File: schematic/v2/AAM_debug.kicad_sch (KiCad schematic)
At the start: 16 parts, among them J16 AAM_DBG, J20 USB_A, U33 CH340G, Y2 Crystal

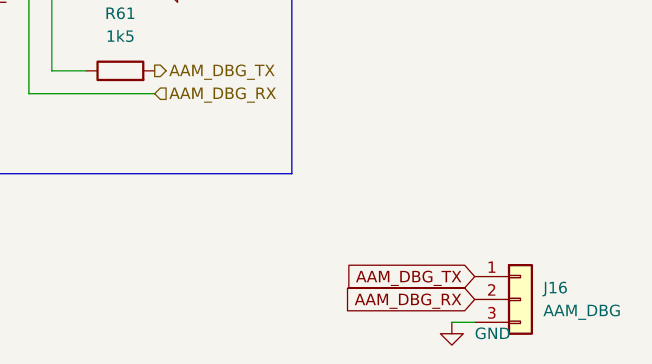
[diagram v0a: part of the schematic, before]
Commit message: progress on putting things in different sheets
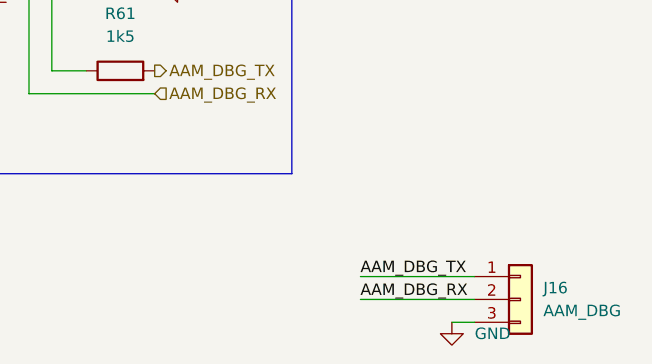
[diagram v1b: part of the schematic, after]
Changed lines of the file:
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@@
+	(wire
+		(pts
+			(xy 179.07 113.03) (xy 191.77 113.03)
+		)
+		(stroke
+			(width 0)
+			(type default)
+		)
+	)
 	(wire
 		(pts
@@
 	(wire
 		(pts
+			(xy 179.07 110.49) (xy 191.77 110.49)
+		)
+		(stroke
+			(width 0)
+			(type default)
+		)
+	)
+	(wire
+		(pts
 			(xy 127 48.26) (xy 127 52.07)
 		)
@@
 		)
 	)
-	(global_label "AAM_DBG_RX"
-		(shape input)
-		(at 191.77 113.03 180)
-		(fields_autoplaced yes)
+	(label "AAM_DBG_RX"
+		(at 179.07 113.03 0)
 		(effects
 			(font
 				(size 1.27 1.27)
 			)
-			(justify right)
-		)
-		(property "Intersheetrefs" "${INTERSHEET_REFS}"
-			(at 176.6292 113.03 0)
-			(effects
-				(font
-					(size 1.27 1.27)
-				)
-				(justify right)
-				(hide yes)
+			(justify left bottom)
+		)
+	)
+	(label "AAM_DBG_TX"
+		(at 179.07 110.49 0)
+		(effects
+			(font
+				(size 1.27 1.27)
 			)
+			(justify left bottom)
 		)
 	)
@@
 				(hide yes)
 			)
-		)
-	)
-	(global_label "AAM_DBG_TX"
-		(shape input)
-		(at 191.77 110.49 180)
-		(fields_autoplaced yes)
-		(effects
-			(font
-				(size 1.27 1.27)
-			)
-			(justify right)
-		)
-		(property "Intersheetrefs" "${INTERSHEET_REFS}"
-			(at 176.9316 110.49 0)
-			(effects
-				(font
-					(size 1.27 1.27)
-				)
-				(justify right)
-				(hide yes)
-			)

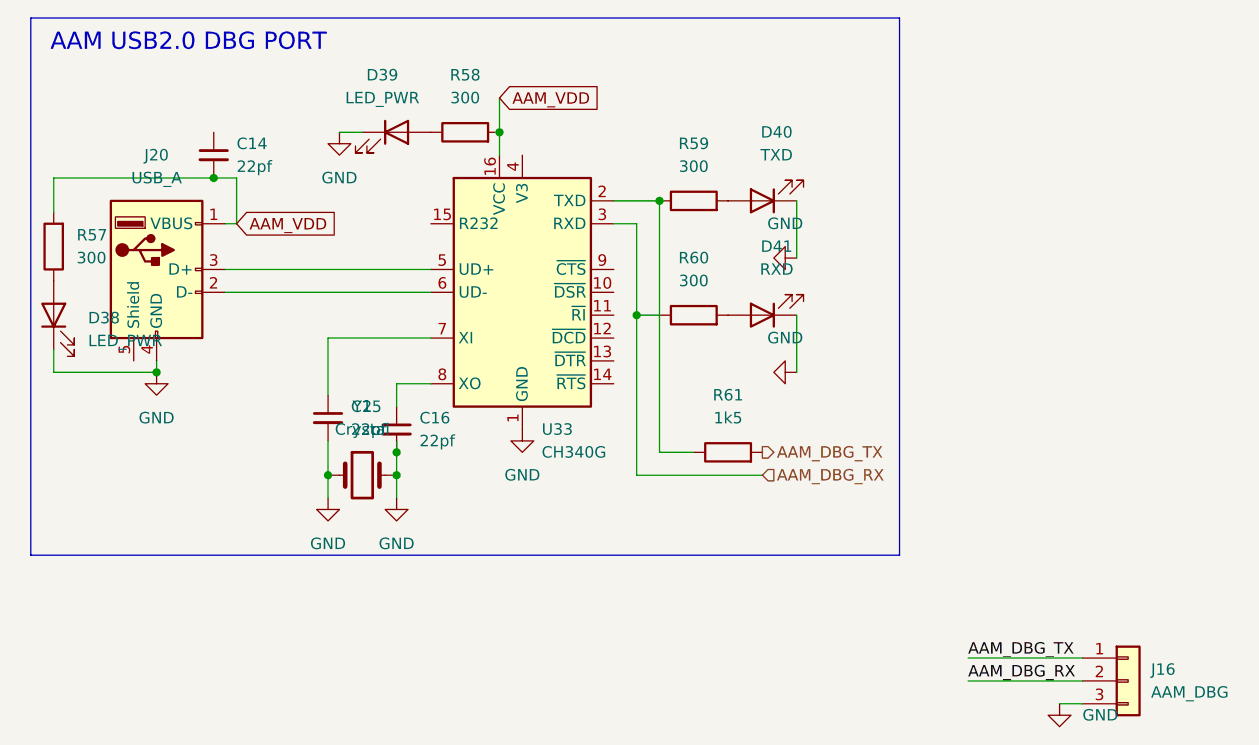
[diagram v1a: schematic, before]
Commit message: v2 updates. remove sniffer
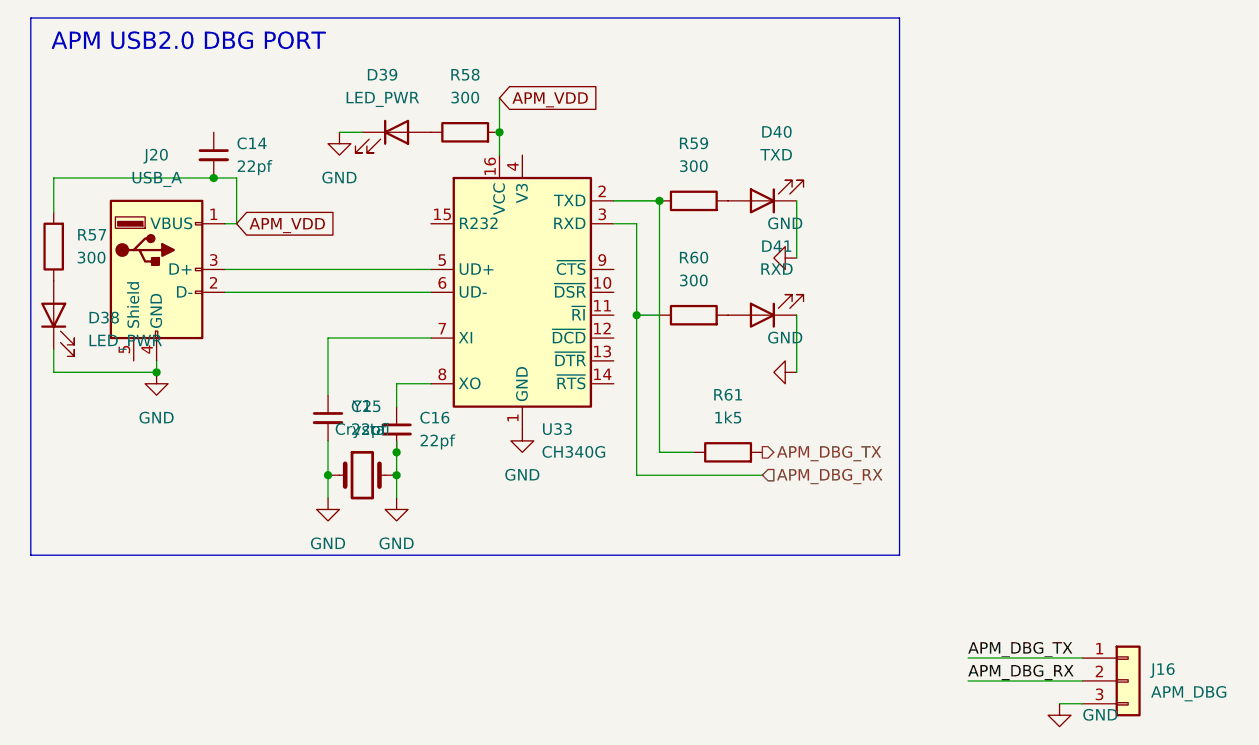
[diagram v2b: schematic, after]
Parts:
- J16: value AAM_DBG -> APM_DBG
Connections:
- net AAM_DBG_RX renamed APM_DBG_RX
- net AAM_DBG_TX renamed APM_DBG_TX
- net AAM_VDD renamed APM_VDD
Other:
- note added: "APM USB2.0 DBG PORT"
- note removed: "AAM USB2.0 DBG PORT"
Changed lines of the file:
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@@
 		)
 	)
-	(text "AAM USB2.0 DBG PORT"
+	(text "APM USB2.0 DBG PORT"
 		(exclude_from_sim no)
 		(at 92.456 42.164 0)
@@
 		)
 	)
-	(label "AAM_DBG_RX"
+	(label "APM_DBG_RX"
 		(at 179.07 113.03 0)
 		(effects
@@
 		)
 	)
-	(label "AAM_DBG_TX"
+	(label "APM_DBG_TX"
 		(at 179.07 110.49 0)
 		(effects
@@
 		)
 	)
-	(global_label "AAM_VDD"
+	(global_label "APM_VDD"
 		(shape input)
 		(at 127 48.26 0)
@@
 		)
 	)
-	(global_label "AAM_VDD"
+	(global_label "APM_VDD"
 		(shape input)
 		(at 97.79 62.23 0)
@@
 		)
 	)
-	(hierarchical_label "AAM_DBG_TX"
+	(hierarchical_label "APM_DBG_TX"
 		(shape output)
 		(at 156.21 87.63 0)
@@
 		)
 	)
-	(hierarchical_label "AAM_DBG_RX"
+	(hierarchical_label "APM_DBG_RX"
 		(shape input)
 		(at 156.21 90.17 0)
@@
 			)
 		)
-		(property "Value" "AAM_DBG"
+		(property "Value" "APM_DBG"
 			(at 199.39 114.2999 0)
 			(effects
